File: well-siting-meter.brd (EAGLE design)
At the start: 93.8 x 65.9 mm, 46 parts, among them J2 7805, T1 MOSFET-NCHANNELFQP30N06L, U1 LCD-16X2NOHOLES, U2 ARDUINO_PRO_MINI, U3 EC2, U4 EC2, U5 AD623, U6 AD623, U7 MAX1771

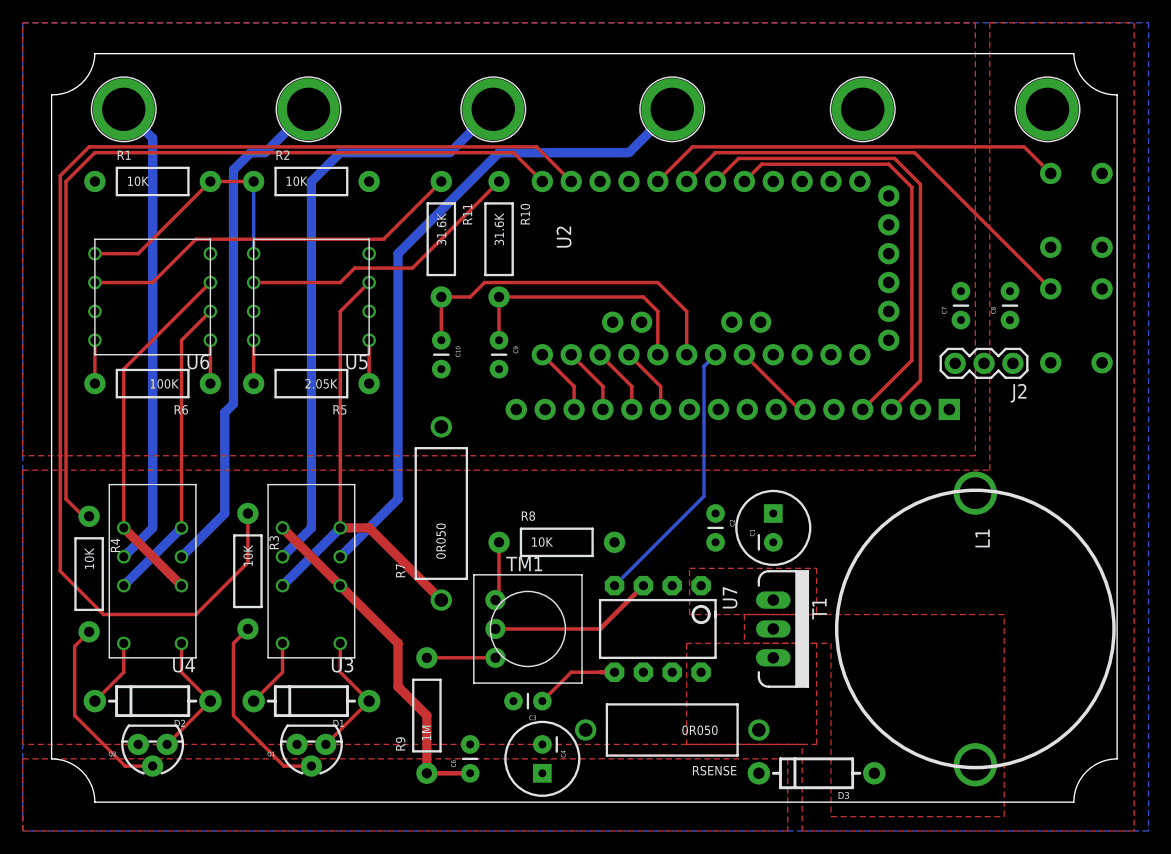
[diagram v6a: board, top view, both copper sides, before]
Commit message: rearranged a few polygons
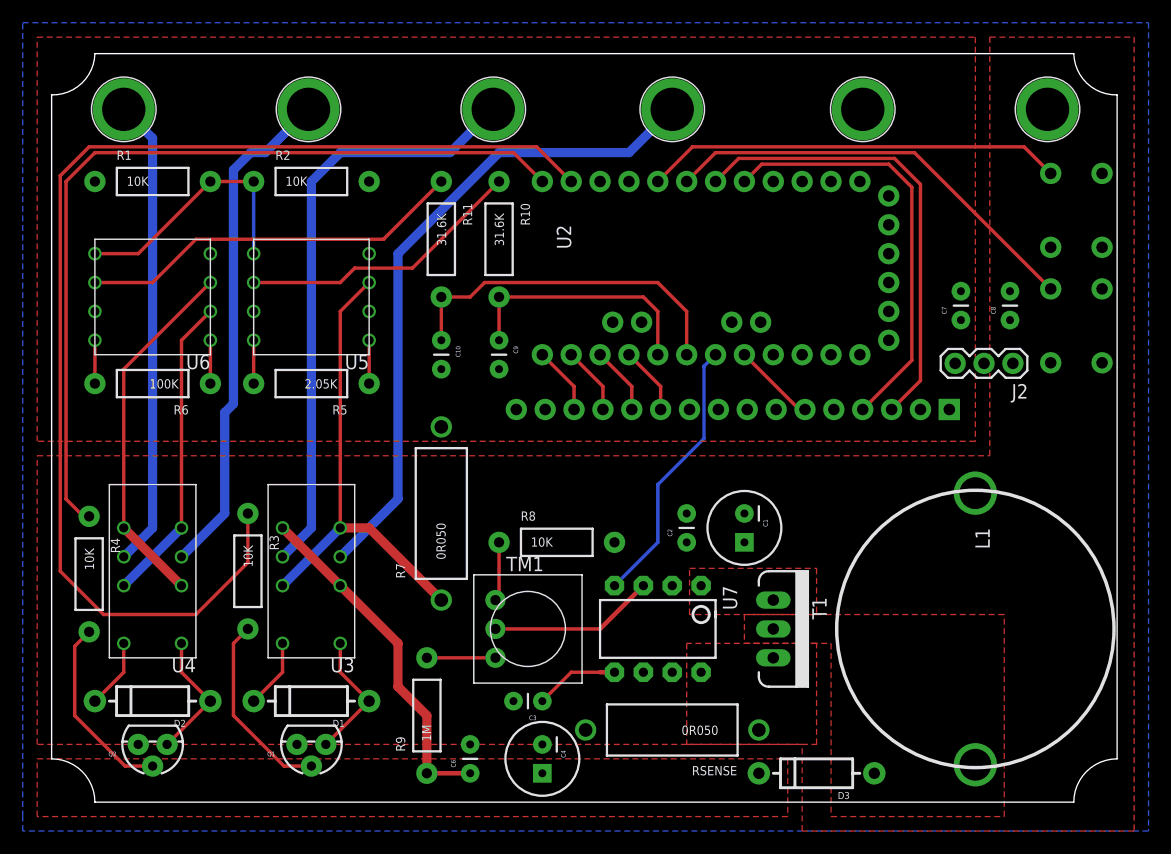
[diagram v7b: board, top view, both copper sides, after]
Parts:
- moved C2 3.59 mm to (57.1, 24.1), turned to 90 degrees
- moved C1 2.54 mm to (62.2, 25.4), turned to 270 degrees
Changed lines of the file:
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@@
 <attribute name="PN" value="SW406-ND" x="91.44" y="53.34" size="1.778" layer="28" rot="MR270" display="off"/>
 </element>
-<element name="C1" library="SparkFun-Passives" package="CPOL-RADIAL-100UF-25V" value="100uF, 35V" x="64.77" y="25.4" rot="R90">
-<attribute name="PN" value="1572-1306-ND" x="64.77" y="25.4" size="1.778" layer="27" rot="R90" display="off"/>
-</element>
-<element name="C2" library="SparkFun-Passives" package="CAP-PTH-SMALL" value="0.1uf" x="59.69" y="26.67" rot="R270">
-<attribute name="PN" value="BC2665CT-ND" x="59.69" y="26.67" size="1.778" layer="27" rot="R270" display="off"/>
+<element name="C1" library="SparkFun-Passives" package="CPOL-RADIAL-100UF-25V" value="100uF, 35V" x="62.23" y="25.4" rot="R270">
+<attribute name="PN" value="1572-1306-ND" x="62.23" y="25.4" size="1.778" layer="27" rot="R270" display="off"/>
+</element>
+<element name="C2" library="SparkFun-Passives" package="CAP-PTH-SMALL" value="0.1uf" x="57.15" y="24.13" rot="R90">
+<attribute name="PN" value="BC2665CT-ND" x="57.15" y="24.13" size="1.778" layer="27" rot="R90" display="off"/>
 </element>
 <element name="C3" library="SparkFun-Passives" package="CAP-PTH-SMALL" value="0.1uf" x="44.45" y="10.16" rot="R180">
@@
 <contactref element="U1" pad="15"/>
 <polygon width="0.3048" layer="1" rank="6">
-<vertex x="-1.27" y="69.85"/>
-<vertex x="82.55" y="69.85"/>
-<vertex x="82.55" y="31.75"/>
-<vertex x="-1.27" y="31.75"/>
+<vertex x="0" y="68.58"/>
+<vertex x="82.55" y="68.58"/>
+<vertex x="82.55" y="33.02"/>
+<vertex x="0" y="33.02"/>
 </polygon>
 </signal>
@@
 <wire x1="38.1" y1="3.81" x2="34.29" y2="3.81" width="0.4064" layer="1"/>
 <polygon width="0.3048" layer="1" thermals="no">
-<vertex x="-1.27" y="-1.27"/>
-<vertex x="-1.27" y="5.08"/>
+<vertex x="0" y="0"/>
+<vertex x="0" y="5.08"/>
 <vertex x="66.04" y="5.08"/>
-<vertex x="66.04" y="-1.27"/>
+<vertex x="66.04" y="0"/>
 </polygon>
 <wire x1="34.29" y1="3.81" x2="34.29" y2="8.89" width="0.8128" layer="1"/>
@@
 <wire x1="21.59" y1="12.7" x2="21.59" y2="15.24" width="0.3048" layer="1"/>
 <polygon width="0.3048" layer="1" rank="6">
-<vertex x="-1.27" y="30.48"/>
-<vertex x="83.82" y="30.48"/>
-<vertex x="83.82" y="69.85"/>
-<vertex x="96.52" y="69.85"/>
+<vertex x="0" y="31.75"/>
+<vertex x="83.82" y="31.75"/>
+<vertex x="83.82" y="68.58"/>
+<vertex x="96.52" y="68.58"/>
 <vertex x="96.52" y="-1.27"/>
 <vertex x="67.31" y="-1.27"/>
 <vertex x="67.31" y="6.35"/>
-<vertex x="-1.27" y="6.35"/>
+<vertex x="0" y="6.35"/>
 </polygon>
 <contactref element="C1" pad="1"/>
@@
 <contactref element="U7" pad="4"/>
 <contactref element="U2" pad="19"/>
-<wire x1="58.674" y1="39.624" x2="58.674" y2="28.194" width="0.3048" layer="16"/>
-<wire x1="58.674" y1="28.194" x2="50.8" y2="20.32" width="0.3048" layer="16"/>
 <wire x1="58.674" y1="39.624" x2="59.69" y2="40.64" width="0.3048" layer="16"/>
+<wire x1="58.674" y1="39.624" x2="58.674" y2="33.274" width="0.3048" layer="16"/>
+<wire x1="58.674" y1="33.274" x2="54.61" y2="29.21" width="0.3048" layer="16"/>
+<wire x1="54.61" y1="29.21" x2="54.61" y2="24.13" width="0.3048" layer="16"/>
+<wire x1="54.61" y1="24.13" x2="50.8" y2="20.32" width="0.3048" layer="16"/>
 </signal>
 <signal name="N$12">

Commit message: prep for mfg
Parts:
- C1: value 100uF, 35V -> 100uF
- C4: value 4u7, 250V -> 4u7
- C6: value 0.1uf, 250V -> 0.1uf
- L1: value MURATA1400 -> 22uH; device murata1400:MURATA1400 -> misc:1415
- moved C3 5.08 mm to (39.4, 10.2)
- moved L1 5.08 mm to (77.5, 16.5)
- moved C1 2.84 mm to (64.8, 26.7)
- moved C8 2.70 mm to (83.8, 45.7)
- moved J2 2.54 mm to (84.3, 41.9)
- moved S1 2.54 mm to (88.9, 43.2)
- moved S2 2.54 mm to (88.9, 53.3)
- moved C7 2.40 mm to (80.0, 45.7)
- moved C4 1.27 mm to (43.2, 5.08)
- moved C6 1.27 mm to (36.8, 3.81)
- moved C2 1.27 mm to (57.1, 25.4)
- moved R8 1.27 mm to (45.7, 25.4)
- moved R9 1.27 mm to (33.0, 8.89)
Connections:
- net N$9: now also L1.P2; no longer L1.P$2
- net V_BATT: now also L1.P1; no longer L1.P$1
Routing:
- net N$7: track 7.40 -> 12.5 mm
- net B2: track 36.8 -> 34.3 mm
- net B1: track 38.0 -> 36.4 mm
- net N$8: track 5.21 -> 6.48 mm
- net N$6: track 6.03 -> 7.30 mm
- net VIN: track 30.7 -> 30.1 mm
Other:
- board text added: "GND"
- board text added: "I1"
- board text added: "I2"
- board text added: "V1"
- board text added: "V2"
- board text added: "VBAT"
- board text added: "danwahl.net/"
- board text added: "v2 | rev - | sn:"
- board text added: "well-siting-meter"
